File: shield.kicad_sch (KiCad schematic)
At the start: 0 parts

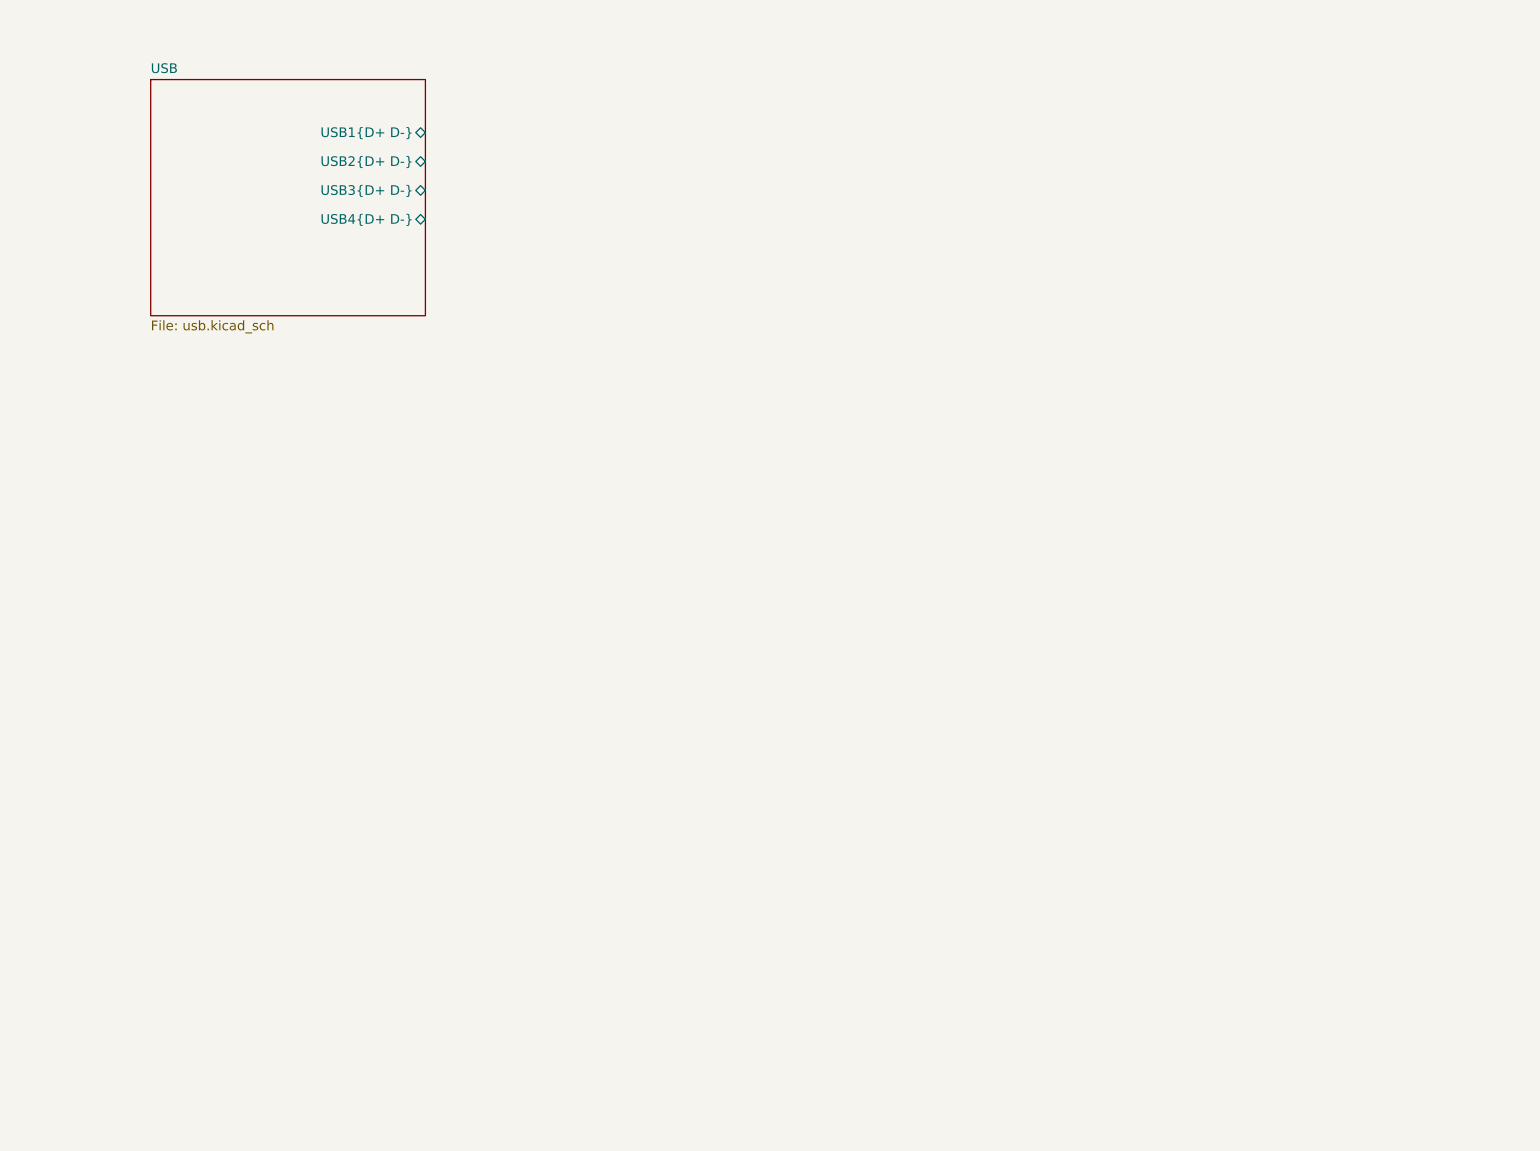
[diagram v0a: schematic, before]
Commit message: Add Uno shield
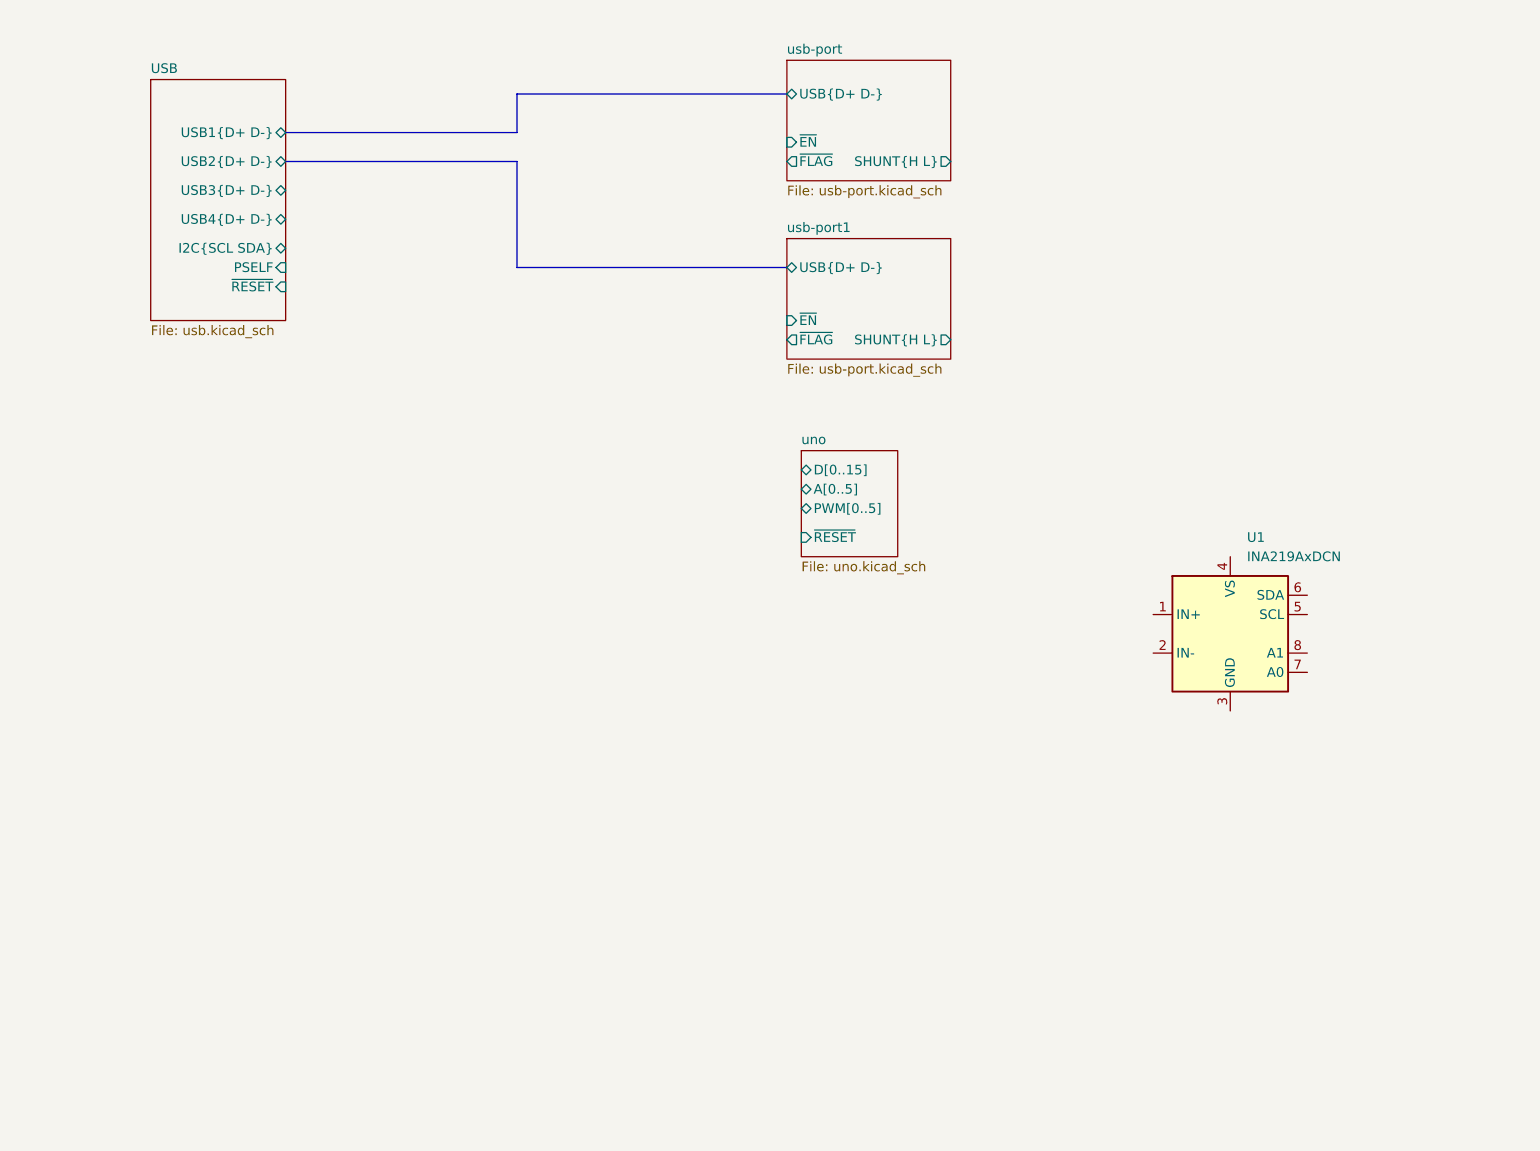
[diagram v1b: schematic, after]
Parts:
- added U1: INA219AxDCN, Package_TO_SOT_SMD:SOT-23-8, symbol Sensor_Energy:INA219AxDCN
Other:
- added sheet uno (uno.kicad_sch)
- added sheet usb-port (usb-port.kicad_sch)
- added sheet usb-port1 (usb-port.kicad_sch)
- sheet USB ports: added I2C{SCL SDA}, PSELF, ~{RESET}; removed none

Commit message: Add RP2350B from example
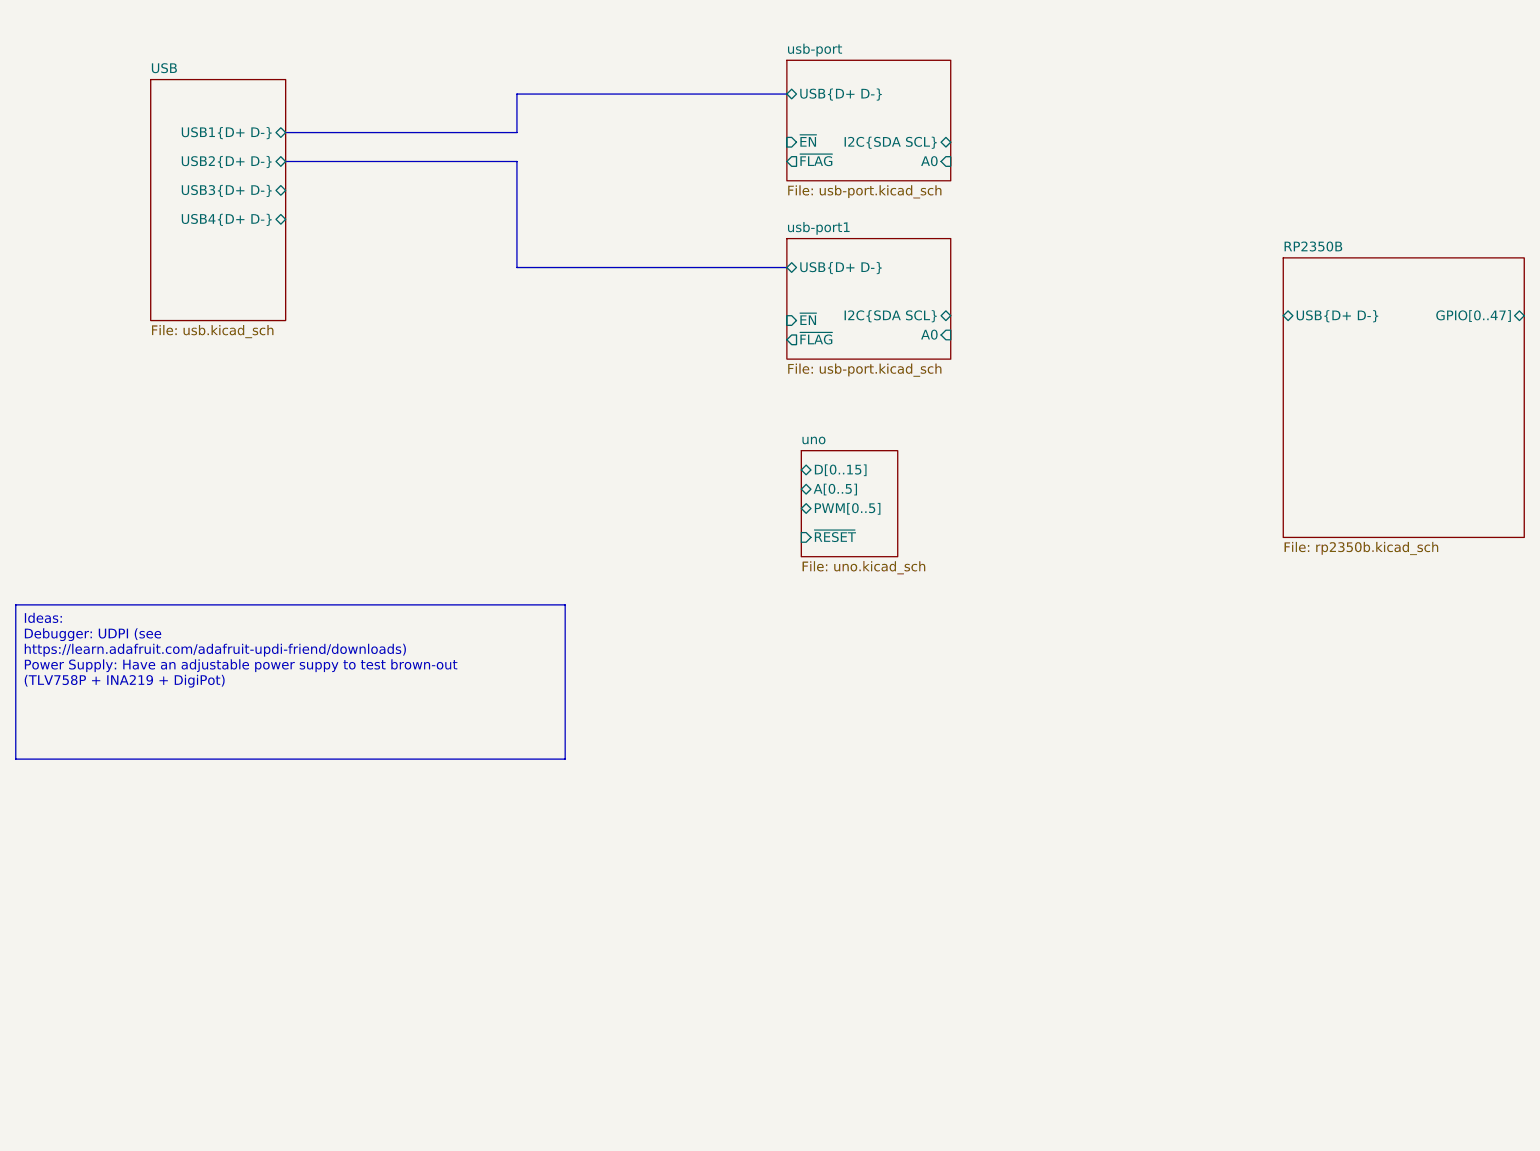
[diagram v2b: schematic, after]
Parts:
- removed U1: INA219AxDCN, Package_TO_SOT_SMD:SOT-23-8, symbol Sensor_Energy:INA219AxDCN
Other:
- added sheet RP2350B (rp2350b.kicad_sch)
- sheet USB ports: added none; removed I2C{SCL SDA}, PSELF, ~{RESET}
- sheet usb-port ports: added A0, I2C{SDA SCL}; removed SHUNT{H L}
- sheet usb-port1 ports: added A0, I2C{SDA SCL}; removed SHUNT{H L}
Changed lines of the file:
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@@
 		)
 	)
-	(symbol
-		(lib_id "Sensor_Energy:INA219AxDCN")
-		(at 193.04 111.76 0)
-		(unit 1)
+	(text_box "Ideas:\nDebugger: UDPI (see https://learn.adafruit.com/adafruit-updi-friend/downloads)\nPower Supply: Have an adjustable power suppy to test brown-out (TLV758P + INA219 + DigiPot)"
 		(exclude_from_sim no)
-		(in_bom yes)
-		(on_board yes)
-		(dnp no)
-		(fields_autoplaced yes)
-		(property "Reference" "U1"
-			(at 195.2341 99.06 0)
-			(effects
-				(font
-					(size 1.27 1.27)
-				)
-				(justify left)
-			)
-		)
-		(property "Value" "INA219AxDCN"
-			(at 195.2341 101.6 0)
-			(effects
-				(font
-					(size 1.27 1.27)
-				)
-				(justify left)
-			)
-		)
-		(property "Footprint" "Package_TO_SOT_SMD:SOT-23-8"
-			(at 209.55 120.65 0)
-			(effects
-				(font
-					(size 1.27 1.27)
-				)
-				(hide yes)
-			)
-		)
-		(property "Datasheet" "http://www.ti.com/lit/ds/symlink/ina219.pdf"
-			(at 201.93 114.3 0)
-			(effects
-				(font
-					(size 1.27 1.27)
-				)
-				(hide yes)
-			)
-		)
-		(property "Description" "Zero-Drift, Bidirectional Current/Power Monitor (0-26V) With I2C Interface, SOT-23-8"
-			(at 193.04 111.76 0)
-			(effects
-				(font
-					(size 1.27 1.27)
-				)
-				(hide yes)
-			)
-		)
-		(property "LCSC" "C87469"
-			(at 193.04 111.76 0)
-			(effects
-				(font
-					(size 1.27 1.27)
-				)
-				(hide yes)
-			)
-		)
-		(pin "6"
-		)
-		(pin "2"
-		)
-		(pin "7"
-		)
-		(pin "1"
-		)
-		(pin "4"
-		)
-		(pin "8"
-		)
-		(pin "5"
-		)
-		(pin "3"
-		)
-		(instances
-			(project ""
-				(path "/d57ea000-ef46-42c0-b86a-7e6b1d4431c2"
-					(reference "U1")
-					(unit 1)
-				)
-			)
+		(at 33.02 107.95 0)
+		(size 72.39 20.32)
+		(stroke
+			(width 0)
+			(type default)
+		)
+		(fill
+			(type none)
+		)
+		(effects
+			(font
+				(size 1.27 1.27)
+			)
+			(justify left top)
 		)
 	)
@@
 			)
 		)
-		(pin "SHUNT{H L}" output
-			(at 156.21 73.025 0)
-			(effects
-				(font
-					(size 1.27 1.27)
-				)
-				(justify right)
-			)
-		)
 		(pin "USB{D+ D-}" bidirectional
 			(at 134.62 63.5 180)
@@
 				)
 				(justify left)
+			)
+		)
+		(pin "A0" input
+			(at 156.21 72.39 0)
+			(effects
+				(font
+					(size 1.27 1.27)
+				)
+				(justify right)
+			)
+		)
+		(pin "I2C{SDA SCL}" bidirectional
+			(at 156.21 69.85 0)
+			(effects
+				(font
+					(size 1.27 1.27)
+				)
+				(justify right)
 			)
 		)
@@
 			)
 		)
-		(pin "PSELF" input
-			(at 68.58 63.5 0)
-			(effects
-				(font
-					(size 1.27 1.27)
-				)
-				(justify right)
-			)
-		)
-		(pin "~{RESET}" input
-			(at 68.58 66.04 0)
-			(effects
-				(font
-					(size 1.27 1.27)
-				)
-				(justify right)
-			)
-		)
-		(pin "I2C{SCL SDA}" bidirectional
-			(at 68.58 60.96 0)
-			(effects
-				(font
-					(size 1.27 1.27)
-				)
-				(justify right)
-			)
-		)
 		(instances
 			(project "shield"
@@
 	)
 	(sheet
+		(at 200.025 62.23)
+		(size 31.75 36.83)
+		(fields_autoplaced yes)
+		(stroke
+			(width 0.1524)
+			(type solid)
+		)
+		(fill
+			(color 0 0 0 0.0000)
+		)
+		(property "Sheetname" "RP2350B"
+			(at 200.025 61.5184 0)
+			(effects
+				(font
+					(size 1.27 1.27)
+				)
+				(justify left bottom)
+			)
+		)
+		(property "Sheetfile" "rp2350b.kicad_sch"
+			(at 200.025 99.6446 0)
+			(effects
+				(font
+					(size 1.27 1.27)
+				)
+				(justify left top)
+			)
+		)
+		(property "Field2" ""
+			(at 200.025 62.23 0)
+			(effects
+				(font
+					(size 1.27 1.27)
+				)
+				(hide yes)
+			)
+		)
+		(pin "USB{D+ D-}" bidirectional
+			(at 200.025 69.85 180)
+			(effects
+				(font
+					(size 1.27 1.27)
+				)
+				(justify left)
+			)
+		)
+		(pin "GPIO[0..47]" bidirectional
+			(at 231.775 69.85 0)
+			(effects
+				(font
+					(size 1.27 1.27)
+				)
+				(justify right)
+			)
+		)
+		(instances
+			(project "shield"
+				(path "/d57ea000-ef46-42c0-b86a-7e6b1d4431c2"
+					(page "6")
+				)
+			)
+		)
+	)
+	(sheet
 		(at 136.525 87.63)
 		(size 12.7 13.97)
@@
 			)
 		)
-		(pin "SHUNT{H L}" output
-			(at 156.21 49.53 0)
-			(effects
-				(font
-					(size 1.27 1.27)
-				)
-				(justify right)
-			)
-		)
 		(pin "USB{D+ D-}" bidirectional
 			(at 134.62 40.64 180)
@@
 			)
 		)
+		(pin "A0" input
+			(at 156.21 49.53 0)
+			(effects
+				(font
+					(size 1.27 1.27)
+				)
+				(justify right)
+			)
+		)
+		(pin "I2C{SDA SCL}" bidirectional
+			(at 156.21 46.99 0)
+			(effects
+				(font
+					(size 1.27 1.27)
+				)
+				(justify right)
+			)
+		)

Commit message: Break out RP2350
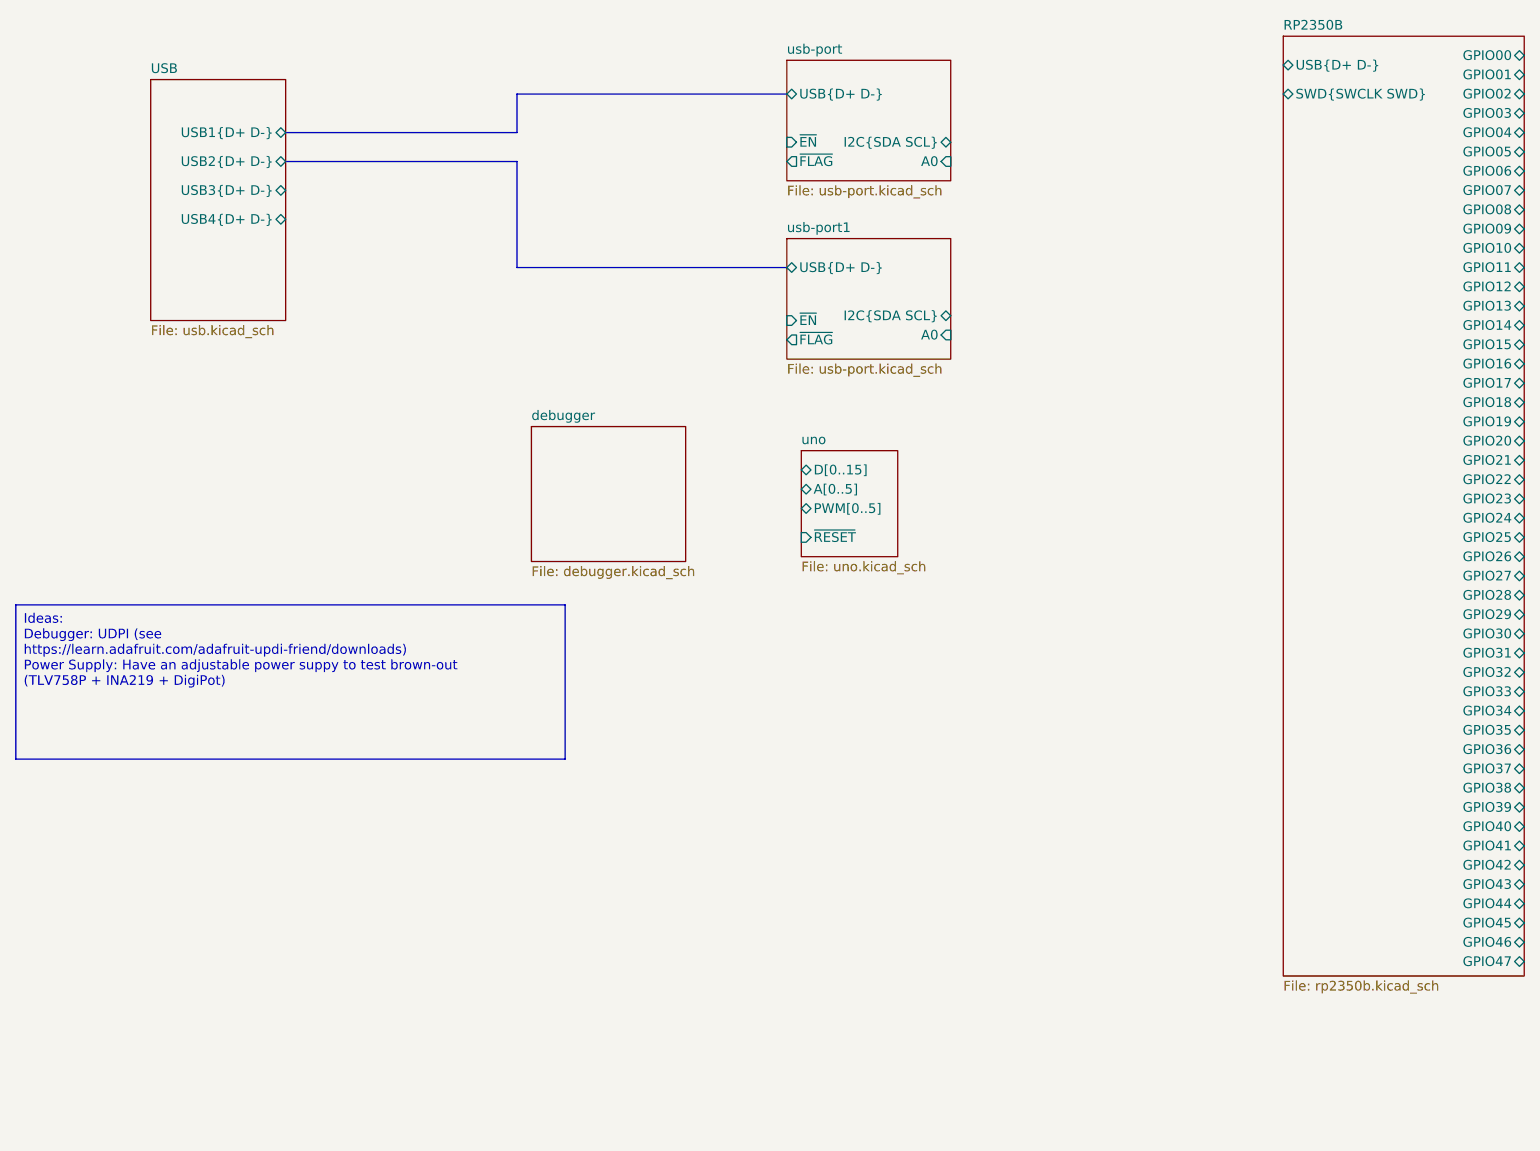
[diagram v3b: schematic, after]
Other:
- added sheet debugger (debugger.kicad_sch)
- sheet RP2350B ports: added GPIO00, GPIO01, GPIO02, GPIO03, GPIO04, GPIO05, GPIO06, GPIO07, GPIO08, GPIO09, GPIO10, GPIO11, GPIO12, GPIO13, GPIO14, GPIO15, GPIO16, GPIO17, GPIO18, GPIO19, GPIO20, GPIO21, GPIO22, GPIO23, GPIO24, GPIO25, GPIO26, GPIO27, GPIO28, GPIO29, GPIO30, GPIO31, GPIO32, GPIO33, GPIO34, GPIO35, GPIO36, GPIO37, GPIO38, GPIO39, GPIO40, GPIO41, GPIO42, GPIO43, GPIO44, GPIO45, GPIO46, GPIO47, SWD{SWCLK SWD}; removed GPIO[0..47]
